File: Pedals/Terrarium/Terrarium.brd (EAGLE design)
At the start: 59.4 x 57.8 mm, 43 parts, among them IC1 TL072CP, IC2 LM78L05

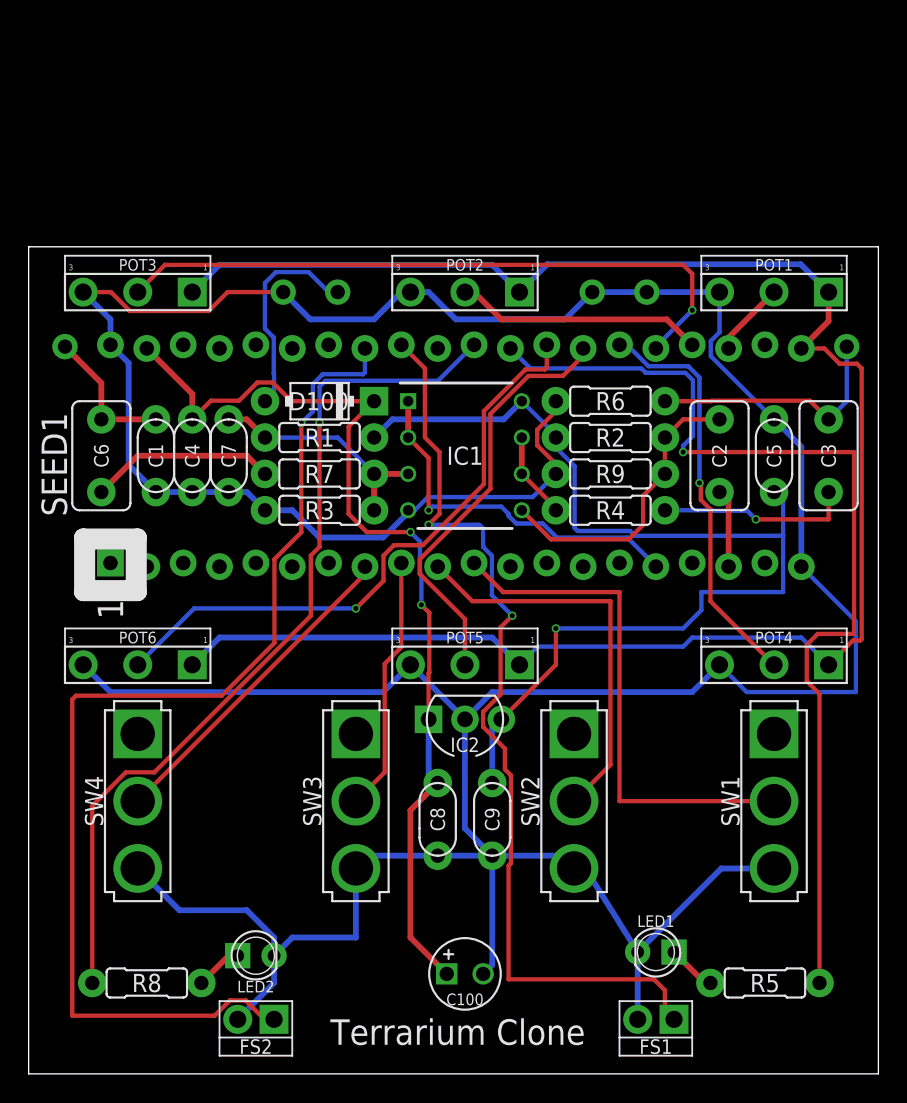
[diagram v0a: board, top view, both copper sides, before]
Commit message: Add true bypass
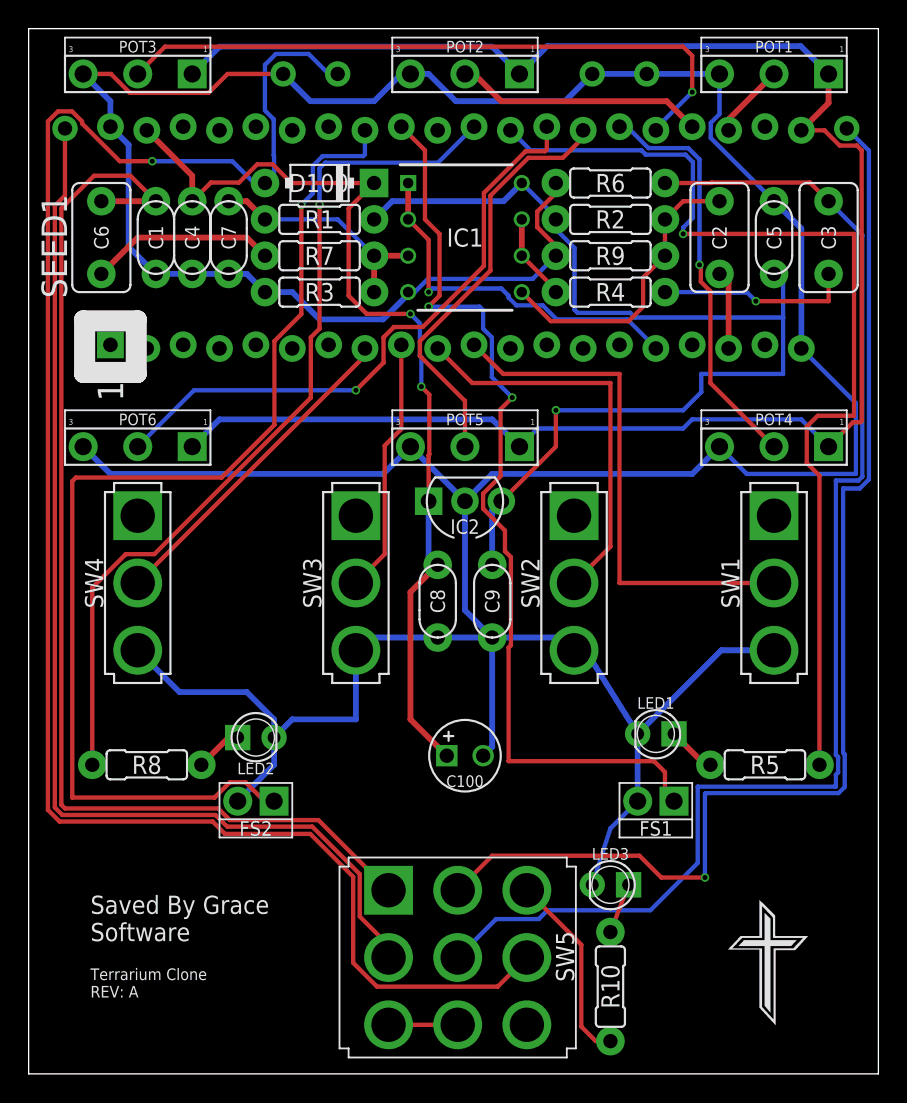
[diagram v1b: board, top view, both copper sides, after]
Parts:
- added LED3: LED.3, diodes:3MM_2
- added R10: 4.7K, resistors:7.5MM.2
- added SW5: 3PDTTOGGLE, switches:3PDT2
- moved IN 15.2 mm to (2.54, 66.0)
- moved OUT 15.2 mm to (57.1, 66.0)
- moved C1 15.2 mm to (8.89, 58.4)
- moved C100 15.2 mm to (30.5, 22.2)
- moved C2 15.2 mm to (48.3, 58.4)
- moved C3 15.2 mm to (55.9, 58.4)
- moved C4 15.2 mm to (11.4, 58.4)
- moved C5 15.2 mm to (52.1, 58.4)
- moved C6 15.2 mm to (5.08, 58.4)
- moved C7 15.2 mm to (14.0, 58.4)
- moved C8 15.2 mm to (28.6, 33.0)
- moved C9 15.2 mm to (32.4, 33.0)
- moved IC1 15.2 mm to (30.5, 58.4)
- moved IC2 15.2 mm to (30.5, 40.0)
- moved R3 15.2 mm to (20.3, 54.6)
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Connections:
- new net BYPASS: SW5.A3, SW5.B3
- new net N$13: IN.P$1, SW5.A2
- new net N$18: OUT.P$1, SW5.B1
- new net N$19: R10.1, SW5.C1
- new net N$20: LED3.ANODE, R10.2
- net GND: now also LED3.P$1
- net N$11: now also SW5.B2; no longer OUT.P$1
- net N$12: now also SW5.A1; no longer IN.P$1
- net N$9: now also SW5.C2
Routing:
- net N$9: track 14.8 -> 123.4 mm, vias 0 -> 1
- net N$18: track 0.00 -> 82.8 mm, vias 0 -> 1
- net N$13: track 0.00 -> 77.6 mm
- net N$11: track 17.6 -> 90.2 mm
- net N$12: track 9.94 -> 79.1 mm
- net N$19: track 0.00 -> 13.6 mm
- net GND: track 282.5 -> 289.3 mm
- net BYPASS: track 0.00 -> 4.83 mm
- net N$20: track 0.00 -> 3.54 mm
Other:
- board size 59.4 x 57.8 mm -> 59.4 x 73 mm
- board text added: "Saved By Grace Software"
- board text added: "Terrarium Clone REV: A"
- board text removed: "Terrarium Clone"
